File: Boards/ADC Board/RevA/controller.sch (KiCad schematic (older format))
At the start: 3 parts

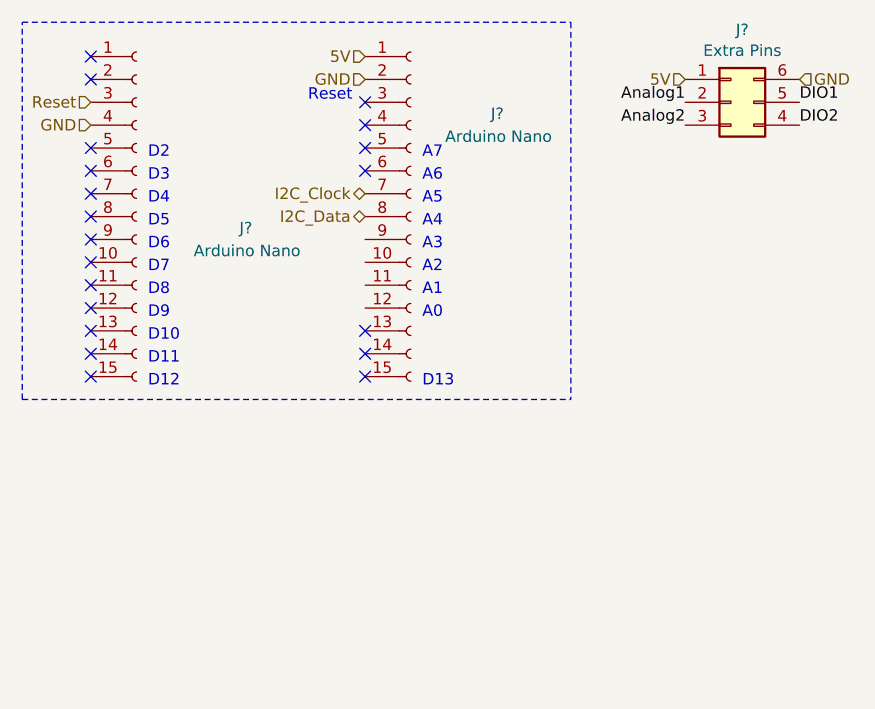
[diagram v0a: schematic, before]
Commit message: Copied controller board from micro board to ADC board. Created pull up/down sheets and populated them.
Also copied over main set of header pins into ADC sheet.
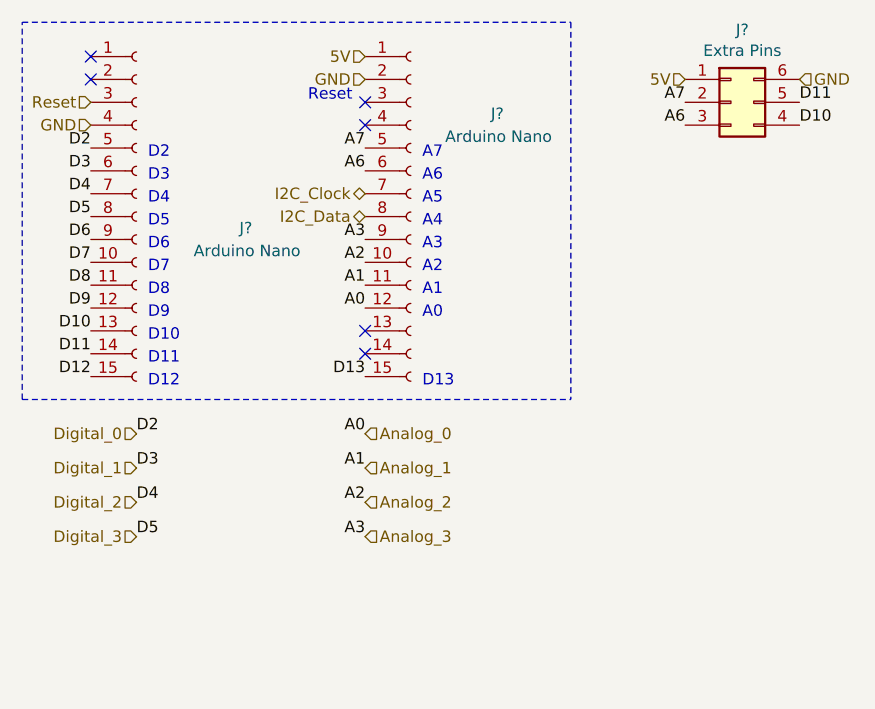
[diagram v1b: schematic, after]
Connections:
- net Analog1 is gone; now on net A7: J?.2 (Pin_2)
- net Analog2 is gone; now on net A6: J?.3 (Pin_3)
- net DIO1 is gone; now on net D11: J?.5 (Pin_5)
- net DIO2 is gone; now on net D10: J?.4 (Pin_4)
- net D7: now reaches J?.10 (Pin_10)
- net D8: now reaches J?.11 (Pin_11)
- net D9: now reaches J?.12 (Pin_12)
- net D10: now reaches J?.13 (Pin_13)
- net D11: now reaches J?.14 (Pin_14)
- net D12: now reaches J?.15 (Pin_15)
- net Digital_0: now reaches J?.5 (Pin_5)
- net Digital_1: now reaches J?.6 (Pin_6)
- net Digital_2: now reaches J?.7 (Pin_7)
- net Digital_3: now reaches J?.8 (Pin_8)
- net D6: now reaches J?.9 (Pin_9)
- net Analog_2: now reaches J?.10 (Pin_10)
- net Analog_1: now reaches J?.11 (Pin_11)
- net Analog_0: now reaches J?.12 (Pin_12)
- net D13: now reaches J?.15 (Pin_15)
- net A7: now reaches J?.5 (Pin_5)
- net A6: now reaches J?.6 (Pin_6)
- net Analog_3: now reaches J?.9 (Pin_9)
- no-connect marks 20 -> 6
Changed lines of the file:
@@
 $Descr A4 11693 8268
 encoding utf-8
-Sheet 2 4
+Sheet 2 6
 Title ""
 Date ""
@@
 NoConn ~ 1400 850
 NoConn ~ 1400 950
-NoConn ~ 1400 1350
-NoConn ~ 1400 1450
-NoConn ~ 1400 1550
-NoConn ~ 1400 1650
-NoConn ~ 1400 1750
-NoConn ~ 1400 1850
-NoConn ~ 1400 1950
 NoConn ~ 2600 2150
 NoConn ~ 2600 2050
-NoConn ~ 2600 1350
-NoConn ~ 2600 1250
 NoConn ~ 2600 1150
 NoConn ~ 2600 1050
@@
 5V
 Text Label 4500 1050 0    50   ~ 0
-DIO1
+D11
 Text Label 4500 1150 0    50   ~ 0
-DIO2
+D10
 Text Label 4000 1050 2    50   ~ 0
-Analog1
+A7
 Text Label 4000 1150 2    50   ~ 0
-Analog2
+A6
 Text HLabel 4500 950  2    50   Input ~ 0
 GND
-NoConn ~ 2600 2250
-NoConn ~ 1400 2050
-NoConn ~ 1400 2150
-NoConn ~ 1400 2250
 Text Notes 2350 1050 0    50   ~ 0
 Reset\n
-NoConn ~ 1400 1250
 Text HLabel 2600 1450 0    50   BiDi ~ 0
 I2C_Clock
@@
 Wire Notes Line
 	3500 700  3500 2350
-Wire Notes Line
-	1100 2350 1100 700
 Text Notes 2850 2300 0    50   ~ 0
 D13
@@
 Wire Notes Line
 	1100 2350 3500 2350
-Wire Notes Line
-	1100 700  3500 700
 Text Notes 1650 1400 0    50   ~ 0
 D3
@@
 Text Notes 1650 1800 0    50   ~ 0
 D7\n
+Text HLabel 1600 2800 0    50   Input ~ 0
+Digital_2
+Text Label 1400 1250 2    50   ~ 0
+D2
+Text Label 1400 1450 2    50   ~ 0
+D4
+Text Label 1400 1550 2    50   ~ 0
+D5
+Text Label 1400 1650 2    50   ~ 0
+D6
+Text Label 1400 1750 2    50   ~ 0
+D7
+Text Label 1400 1850 2    50   ~ 0
+D8
+Text Label 1400 1350 2    50   ~ 0
+D3
+Wire Notes Line
+	1100 700  3500 700
+Wire Notes Line
+	1100 2350 1100 700
+Text Label 1400 1950 2    50   ~ 0
+D9
+Text Label 1400 2050 2    50   ~ 0
+D10
+Text Label 2600 2250 2    50   ~ 0
+D13
+Text Label 1400 2250 2    50   ~ 0
+D12
+Text Label 1400 2150 2    50   ~ 0
+D11
+Text Label 2600 1950 2    50   ~ 0
+A0
+Text Label 2600 1850 2    50   ~ 0
+A1
+Text Label 2600 1650 2    50   ~ 0
+A3
+Text Label 2600 1750 2    50   ~ 0
+A2
+Text Label 2600 1250 2    50   ~ 0
+A7
+Text Label 2600 1350 2    50   ~ 0
+A6
+Text HLabel 1600 2650 0    50   Input ~ 0
+Digital_1
+Text HLabel 1600 2950 0    50   Input ~ 0
+Digital_3
+Text HLabel 1600 2500 0    50   Input ~ 0
+Digital_0
+Text HLabel 2600 2500 2    50   Input ~ 0
+Analog_0
+Text HLabel 2600 2650 2    50   Input ~ 0
+Analog_1
+Text HLabel 2600 2800 2    50   Input ~ 0
+Analog_2
+Text HLabel 2600 2950 2    50   Input ~ 0
+Analog_3
+Text Label 1600 2500 0    50   ~ 0
+D2
+Text Label 1600 2800 0    50   ~ 0
+D4
+Text Label 1600 2950 0    50   ~ 0
+D5
+Text Label 1600 2650 0    50   ~ 0
+D3
+Text Label 2600 2500 2    50   ~ 0
+A0
+Text Label 2600 2650 2    50   ~ 0
+A1
+Text Label 2600 2950 2    50   ~ 0
+A3
+Text Label 2600 2800 2    50   ~ 0
+A2
 $EndSCHEMATC

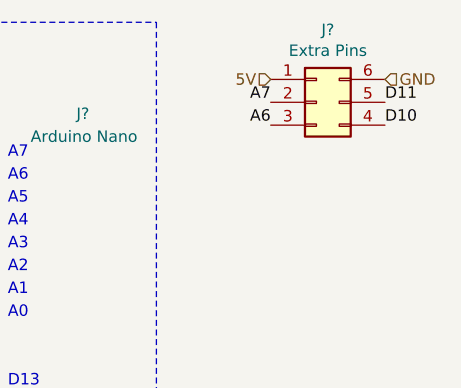
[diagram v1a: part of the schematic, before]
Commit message: Created analog in sheets on ADC board, populated them, and connected them to controller.  Defined Interconnect pins. Placed mounting holes.
Converted some strain gauge connections to nets.
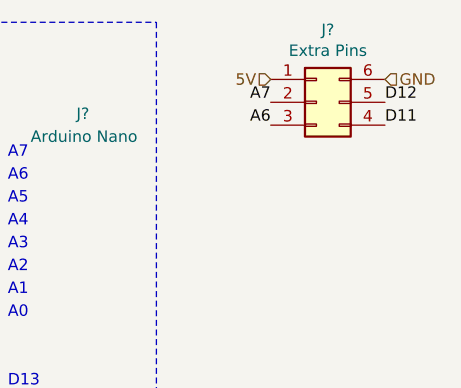
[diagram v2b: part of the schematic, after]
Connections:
- net D10: no longer J?.4 (Pin_4)
- net D11: now also J?.4 (Pin_4); no longer J?.5 (Pin_5)
- net D12: now also J?.5 (Pin_5)
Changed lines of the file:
@@
 $Descr A4 11693 8268
 encoding utf-8
-Sheet 2 6
+Sheet 6 10
 Title ""
 Date ""
@@
 5V
 Text Label 4500 1050 0    50   ~ 0
+D12
+Text Label 4500 1150 0    50   ~ 0
 D11
-Text Label 4500 1150 0    50   ~ 0
-D10
 Text Label 4000 1050 2    50   ~ 0
 A7

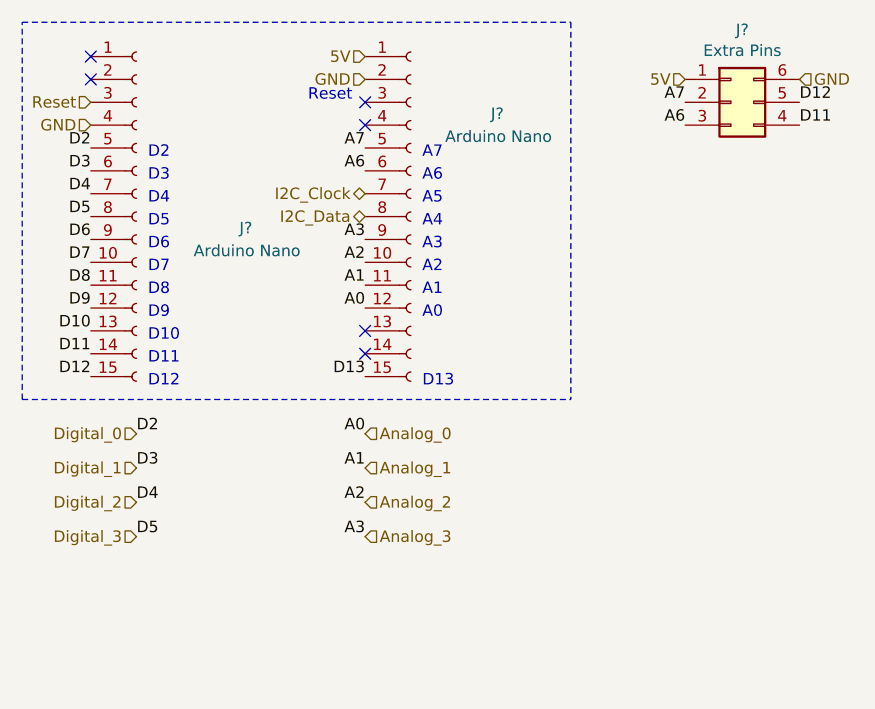
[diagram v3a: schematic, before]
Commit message: Connected power regulator to ADC and micro boards. Added no connects to headers on ADC board. Preformed some footprinting operations on ADC board.
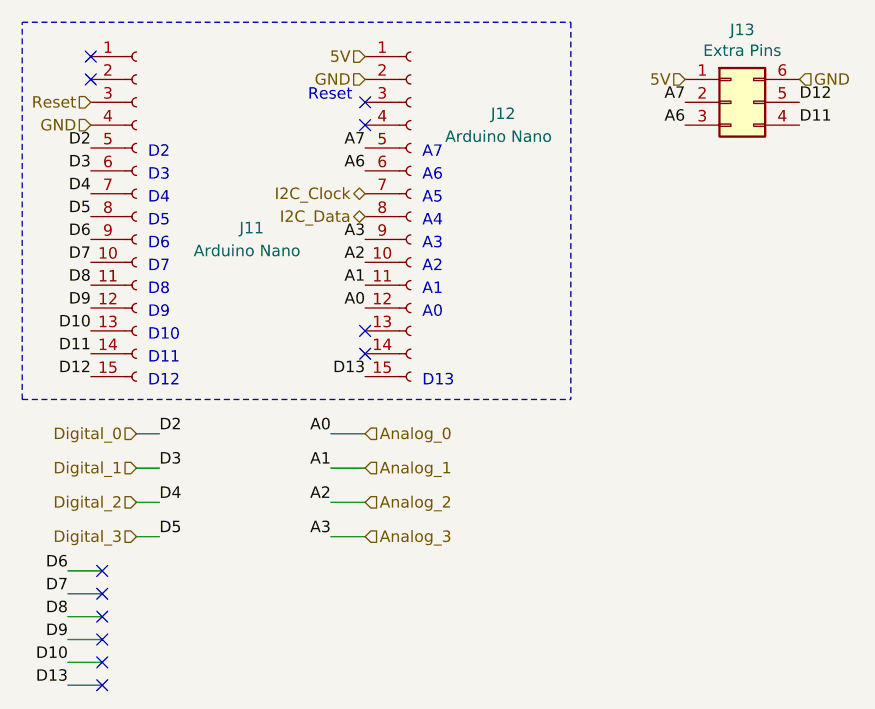
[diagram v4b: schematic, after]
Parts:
- gave numbers to parts that had none: 3
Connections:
- no-connect marks 6 -> 12
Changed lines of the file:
@@
 $EndDescr
 $Comp
-L Connector:Conn_01x15_Female J?
+L Connector:Conn_01x15_Female J11
 U 1 1 614FE43E
 P 1600 1550
-F 0 "J?" H 2050 1500 50  0000 L CNN
+F 0 "J11" H 2050 1500 50  0000 L CNN
 F 1 "Arduino Nano" H 1850 1400 50  0000 L CNN
 F 2 "" H 1600 1550 50  0001 C CNN
@@
 NoConn ~ 2600 1050
 $Comp
-L Connector:Conn_01x15_Female J?
+L Connector:Conn_01x15_Female J12
 U 1 1 61504D87
 P 2800 1550
-F 0 "J?" H 3150 2000 50  0000 L CNN
+F 0 "J12" H 3150 2000 50  0000 L CNN
 F 1 "Arduino Nano" H 2950 1900 50  0000 L CNN
 F 2 "" H 2800 1550 50  0001 C CNN
@@
 $EndComp
 $Comp
-L Connector_Generic:Conn_02x03_Counter_Clockwise J?
+L Connector_Generic:Conn_02x03_Counter_Clockwise J13
 U 1 1 61567E78
 P 4200 1050
-F 0 "J?" H 4250 1367 50  0000 C CNN
+F 0 "J13" H 4250 1367 50  0000 C CNN
 F 1 "Extra Pins" H 4250 1276 50  0000 C CNN
 F 2 "" H 4200 1050 50  0001 C CNN
@@
 Text HLabel 2600 2950 2    50   Input ~ 0
 Analog_3
-Text Label 1600 2500 0    50   ~ 0
+Text Label 1700 2500 0    50   ~ 0
 D2
-Text Label 1600 2800 0    50   ~ 0
+Text Label 1700 2800 0    50   ~ 0
 D4
-Text Label 1600 2950 0    50   ~ 0
+Text Label 1700 2950 0    50   ~ 0
 D5
-Text Label 1600 2650 0    50   ~ 0
+Text Label 1700 2650 0    50   ~ 0
 D3
-Text Label 2600 2500 2    50   ~ 0
+Text Label 2450 2500 2    50   ~ 0
 A0
-Text Label 2600 2650 2    50   ~ 0
+Text Label 2450 2650 2    50   ~ 0
 A1
-Text Label 2600 2950 2    50   ~ 0
+Text Label 2450 2950 2    50   ~ 0
 A3
-Text Label 2600 2800 2    50   ~ 0
+Text Label 2450 2800 2    50   ~ 0
 A2
+Wire Wire Line
+	2450 2500 2600 2500
+Wire Wire Line
+	2450 2650 2600 2650
+Wire Wire Line
+	2600 2800 2450 2800
+Wire Wire Line
+	2450 2950 2600 2950
+Wire Wire Line
+	1700 2500 1600 2500
+Wire Wire Line
+	1700 2650 1600 2650
+Wire Wire Line
+	1700 2800 1600 2800
+Wire Wire Line
+	1700 2950 1600 2950
+Text Label 1300 3300 2    50   ~ 0
+D8
+Text Label 1300 3400 2    50   ~ 0
+D9
+Text Label 1300 3500 2    50   ~ 0
+D10
+Text Label 1300 3600 2    50   ~ 0
+D13
+Text Label 1300 3200 2    50   ~ 0
+D7
+NoConn ~ 1450 3200
+NoConn ~ 1450 3300
+NoConn ~ 1450 3400
+NoConn ~ 1450 3500
+NoConn ~ 1450 3600
+Wire Wire Line
+	1450 3200 1300 3200
+Wire Wire Line
+	1450 3300 1300 3300
+Wire Wire Line
+	1450 3400 1300 3400
+Wire Wire Line
+	1450 3500 1300 3500
+Wire Wire Line
+	1450 3600 1300 3600
+Text Label 1300 3100 2    50   ~ 0
+D6
+NoConn ~ 1450 3100
+Wire Wire Line
+	1450 3100 1300 3100
 $EndSCHEMATC

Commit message: Completed footprint associations for ADC board. Generated netlist for ADC board. Started PCB design for ADC board.
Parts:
- J11, J12: footprint (none) -> Connector_PinSocket_2.54mm:PinSocket_1x15_P2.54mm_Vertical
- J13: footprint (none) -> Connector_PinHeader_2.54mm:PinHeader_2x03_P2.54mm_Vertical
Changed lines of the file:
@@
 F 0 "J11" H 2050 1500 50  0000 L CNN
 F 1 "Arduino Nano" H 1850 1400 50  0000 L CNN
-F 2 "" H 1600 1550 50  0001 C CNN
+F 2 "Connector_PinSocket_2.54mm:PinSocket_1x15_P2.54mm_Vertical" H 1600 1550 50  0001 C CNN
 F 3 "~" H 1600 1550 50  0001 C CNN
 	1    1600 1550
@@
 F 0 "J12" H 3150 2000 50  0000 L CNN
 F 1 "Arduino Nano" H 2950 1900 50  0000 L CNN
-F 2 "" H 2800 1550 50  0001 C CNN
+F 2 "Connector_PinSocket_2.54mm:PinSocket_1x15_P2.54mm_Vertical" H 2800 1550 50  0001 C CNN
 F 3 "~" H 2800 1550 50  0001 C CNN
 	1    2800 1550
@@
 F 0 "J13" H 4250 1367 50  0000 C CNN
 F 1 "Extra Pins" H 4250 1276 50  0000 C CNN
-F 2 "" H 4200 1050 50  0001 C CNN
+F 2 "Connector_PinHeader_2.54mm:PinHeader_2x03_P2.54mm_Vertical" H 4200 1050 50  0001 C CNN
 F 3 "~" H 4200 1050 50  0001 C CNN
 	1    4200 1050
